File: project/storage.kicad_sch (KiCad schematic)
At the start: 53 parts

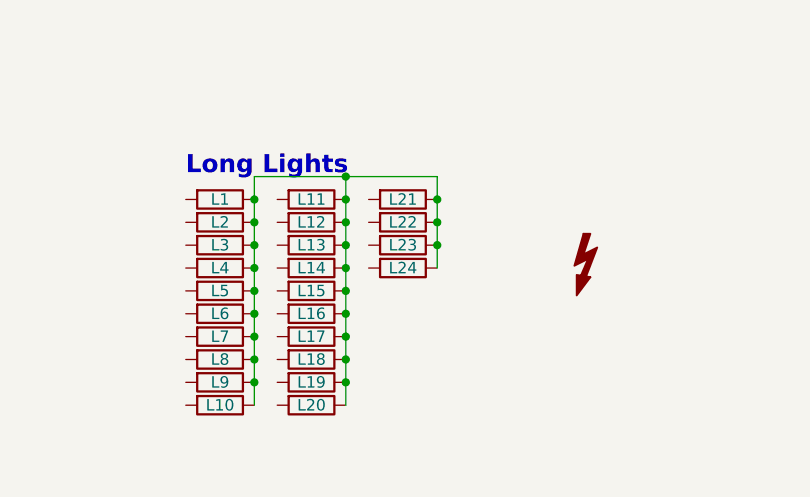
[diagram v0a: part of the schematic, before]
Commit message: adding comunication cable numbers
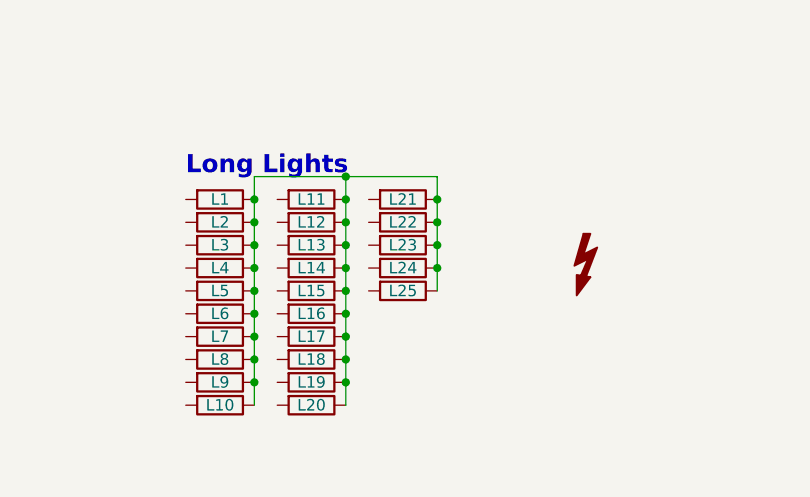
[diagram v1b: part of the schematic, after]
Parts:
- added L25: light, -local:light_long, symbol Device:R
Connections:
- net at L1.1, L10.1, L11.1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: now also L25.1
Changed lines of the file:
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@@
   (junction (at 157.48 172.72) (diameter 0) (color 0 0 0 0)
   )
+  (junction (at 167.64 172.72) (diameter 0) (color 0 0 0 0)
+  )
   (junction (at 147.32 165.1) (diameter 0) (color 0 0 0 0)
   )
@@
   )
   (wire (pts (xy 157.48 170.18) (xy 157.48 172.72))
+    (stroke (width 0) (type default) (color 0 0 0 0))
+  )
+  (wire (pts (xy 167.64 172.72) (xy 167.64 175.26))
     (stroke (width 0) (type default) (color 0 0 0 0))
   )
@@
     (pin "2")
   )
+  (symbol (lib_id "Device:R") (at 163.83 175.26 270) (unit 1)
+    (in_bom yes) (on_board yes)
+    (property "Reference" "L25" (id 0) (at 163.83 175.26 90))
+    (property "Value" "light" (id 1) (at 168.91 175.26 90)
+      (effects (font (size 1.27 1.27)) (justify left top) hide)
+    )
+    (property "Footprint" "-local:light_long" (id 2) (at 167.64 172.72 90)
+      (effects (font (size 1.27 1.27)) (justify left top) hide)
+    )
+    (property "Datasheet" "~" (id 3) (at 163.83 175.26 0)
+      (effects (font (size 1.27 1.27)) hide)
+    )
+    (pin "1")
+    (pin "2")
+  )
   (symbol (lib_id "Device:R") (at 29.21 171.45 270) (unit 1)
     (in_bom yes) (on_board yes)
@@
       (reference "L24") (unit 1) (value "light") (footprint "-local:light_long")
     )
+    (path "/f304c92e-6dc5-4b3b-a433-77e0db203002"
+      (reference "L25") (unit 1) (value "light") (footprint "-local:light_long")
+    )
     (path "/c002752c-95b7-4d22-97b5-311734358824"
